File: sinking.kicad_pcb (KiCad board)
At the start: 2 copper layers, 1 part

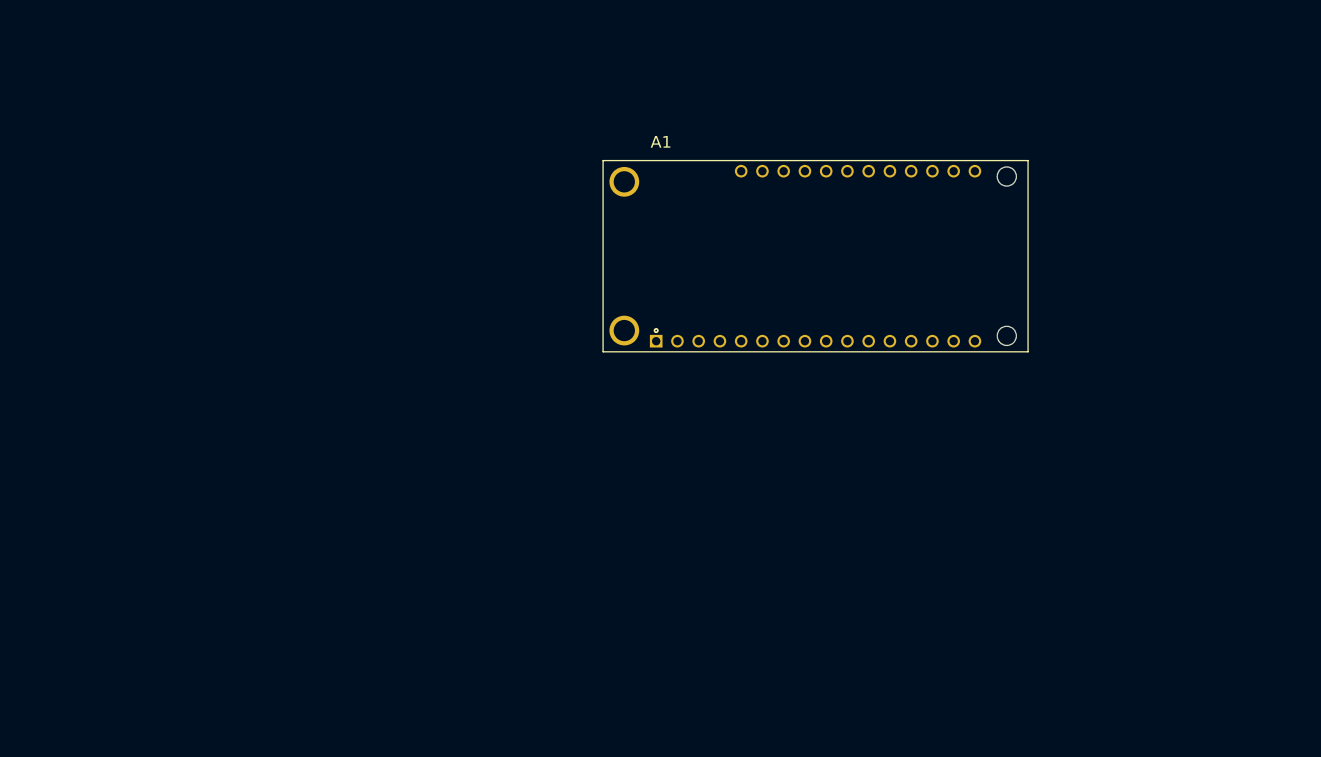
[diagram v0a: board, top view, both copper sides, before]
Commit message: improve pump input filter. add simulation
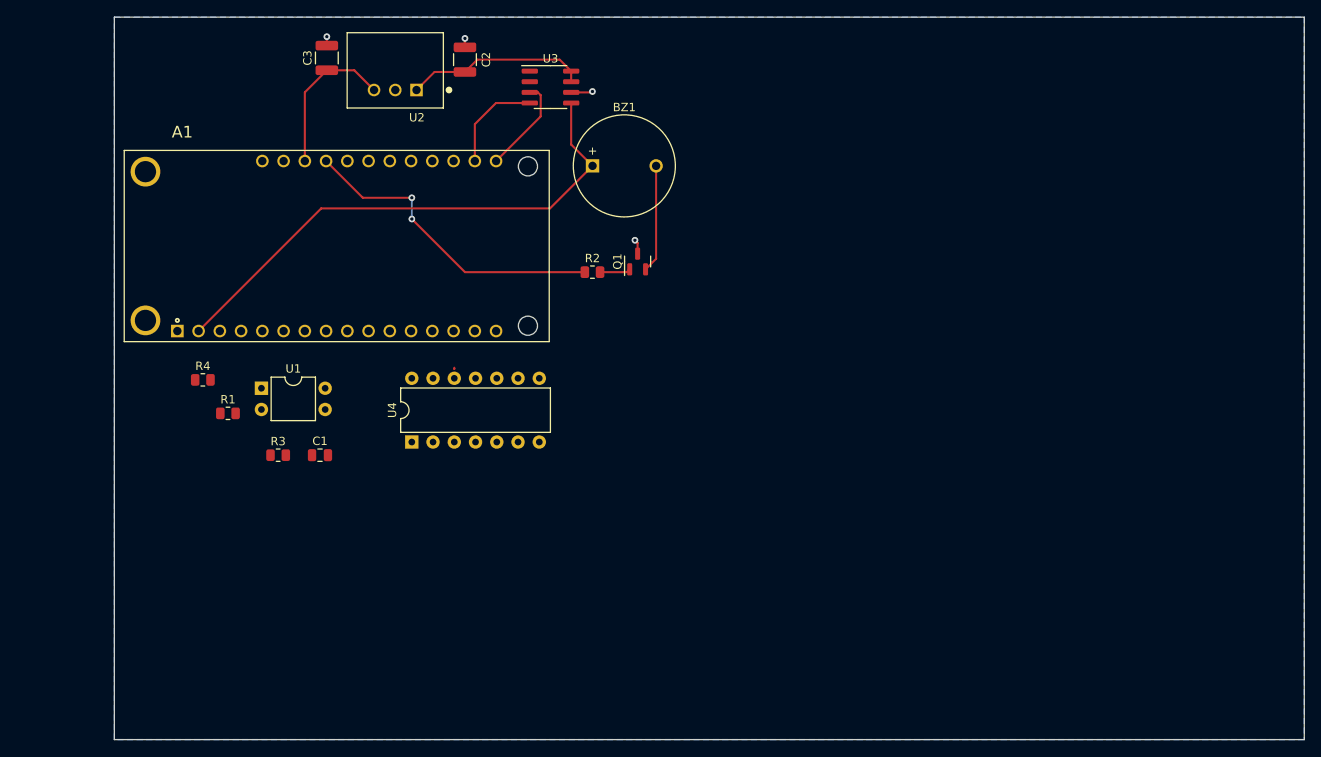
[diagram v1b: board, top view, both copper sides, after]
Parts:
- added BZ1: Buzzer, Buzzer_Beeper:MagneticBuzzer_ProSignal_ABI-009-RC, F.Cu at (115.6, 58.4)
- added C1: 1u, Capacitor_SMD:C_0805_2012Metric, F.Cu at (83.0, 93.0)
- added C2: 10u, Capacitor_SMD:C_1210_3225Metric, F.Cu at (100.3, 45.7)
- added C3: 22u, Capacitor_SMD:C_1210_3225Metric, F.Cu at (83.8, 45.5)
- added Q1: Q_NPN_BCE, Package_TO_SOT_SMD:SOT-23, F.Cu at (121.0, 69.8)
- added R1: 5k, Resistor_SMD:R_0805_2012Metric, F.Cu at (72.0, 88.0)
- added R2: 1k, Resistor_SMD:R_0805_2012Metric, F.Cu at (115.6, 71.1)
- added R3: 10k, Resistor_SMD:R_0805_2012Metric, F.Cu at (78.0, 93.0)
- added R4: 5k, Resistor_SMD:R_0805_2012Metric, F.Cu at (69.0, 84.0)
- added U1: LTV-817, Package_DIP:DIP-4_W7.62mm, F.Cu at (76.0, 85.0)
- added U2: V7805-1000, libs:CONV_V7805-1000, F.Cu at (92.0, 47.0)
- added U3: INA219AxD, Package_SO:SOIC-8_3.9x4.9mm_P1.27mm, F.Cu at (110.6, 49.0)
- added U4: 74HC14, Package_DIP:DIP-14_W7.62mm, F.Cu at (94.0, 91.4)
- moved A1 57.3 mm to (85.0, 68.0)
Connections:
- A1 pad 3V3: unconnected-(A1-Pad3V3) -> +3V3
- A1 pad D2: unconnected-(A1-SDA1_UART1_RTS_SPI1_SCK_PWM3_P1.01_2-PadD2) -> Net-(A1-SDA1_UART1_RTS_SPI1_SCK_PWM3_P1.01_2)
- A1 pad D8: unconnected-(A1-UART2_RTS_PWM1_P1.03_8-PadD8) -> Net-(A1-UART2_RTS_PWM1_P1.03_8)
- A1 pad GND: unconnected-(A1-PadGND) -> GND
- A1 pad SCL: unconnected-(A1-1_SCL_P0.27-PadSCL) -> Net-(A1-1_SCL_P0.27)
- A1 pad SDA: unconnected-(A1-0_SDA_P0.26-PadSDA) -> Net-(A1-0_SDA_P0.26)
- A1 pad VUSB: unconnected-(A1-VBUS-PadVUSB) -> VUSB
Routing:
- net +3V3: track 0.00 -> 63.8 mm
- net Net-(A1-UART2_RTS_PWM1_P1.03_8): track 0.00 -> 37.9 mm, vias 0 -> 2
- net +12V: track 0.00 -> 22.2 mm
- net VUSB: track 0.00 -> 18.6 mm
- net Net-(BZ1--): track 0.00 -> 12.9 mm
- net Net-(A1-1_SCL_P0.27): track 0.00 -> 12.0 mm
- net Net-(A1-0_SDA_P0.26): track 0.00 -> 11.5 mm
- net GND: track 0.00 -> 6.45 mm, vias 0 -> 4
- net Net-(Q1-B): track 0.00 -> 3.68 mm
- added copper zone on B.Cu, net GND
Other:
- board outline added: 142.2 x 86.4 mm

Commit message: first layout
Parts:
- removed C3: 22u, Capacitor_SMD:C_1210_3225Metric
- removed R2: 1k, Resistor_SMD:R_0805_2012Metric
- removed R3: 10k, Resistor_SMD:R_0805_2012Metric
- removed R4: 5k, Resistor_SMD:R_0805_2012Metric
- added C10: 0.1u, Capacitor_SMD:C_1210_3225Metric, F.Cu at (165.1, 95.2)
- added C11: 0.1u, Capacitor_SMD:C_1210_3225Metric, F.Cu at (164.9, 80.6)
- added C12: 1u, Capacitor_SMD:C_0805_2012Metric, F.Cu at (133.4, 104.8)
- added C13: 1u, Capacitor_SMD:C_0805_2012Metric, F.Cu at (133.4, 111.2)
- added C6: 4.7u, Capacitor_SMD:C_0805_2012Metric, F.Cu at (133.1, 66.7)
- added C7: 4.7u, Capacitor_SMD:C_0805_2012Metric, F.Cu at (126.1, 66.7)
- added C8: 4.7u, Capacitor_SMD:C_0805_2012Metric, B.Cu at (122.9, 67.3)
- added C9: 4.7u, Capacitor_SMD:C_0805_2012Metric, B.Cu at (123.2, 73.0)
- added D1: PMEG2005, Package_TO_SOT_SMD:SOT-23_Handsoldering, F.Cu at (133.4, 100.0)
- added J1: 1861975, 1891975:CONN_1861975, F.Cu at (121.4, 77.7)
- added J2: 1861975, 1891975:CONN_1861975, F.Cu at (177.2, 90.8)
- added J3: 1861946, 1891946:CONN_1861946, F.Cu at (177.2, 103.5)
- added J4: SM04B-SRSS-TB, Connector_JST:JST_SH_SM04B-SRSS-TB_1x04-1MP_P1.00mm_Horizontal, F.Cu at (166.4, 65.4)
- added JP1: SolderJumper_3_Open, Jumper:SolderJumper-3_P2.0mm_Open_TrianglePad1.0x1.5mm, B.Cu at (141.7, 76.7)
- added R10: 2.2k, Resistor_SMD:R_0805_2012Metric, F.Cu at (122.9, 68.6)
- added R11: 4.7k, Resistor_SMD:R_0805_2012Metric, B.Cu at (146.5, 78.0)
- added R12: 2.2k, Resistor_SMD:R_0805_2012Metric, F.Cu at (126.1, 69.2)
- added R13: 2.2k, Resistor_SMD:R_0805_2012Metric, B.Cu at (120.0, 69.2)
- added R14: 4.7k, Resistor_SMD:R_0805_2012Metric, B.Cu at (146.5, 81.4)
- added R15: 2.2k, Resistor_SMD:R_0805_2012Metric, B.Cu at (122.9, 69.8)
- added R16: 2.2k, Resistor_SMD:R_0805_2012Metric, B.Cu at (120.1, 74.0)
- added R17: 4.7k, Resistor_SMD:R_0805_2012Metric, B.Cu at (146.5, 84.8)
- added R18: 2.2k, Resistor_SMD:R_0805_2012Metric, B.Cu at (123.2, 75.6)
- added R19: 10k, Resistor_SMD:R_0805_2012Metric, F.Cu at (151.1, 73.9)
- added R20: 10k, Resistor_SMD:R_0805_2012Metric, F.Cu at (151.1, 77.7)
- added R21: 0.1, Resistor_SMD:R_2512_6332Metric, F.Cu at (171.5, 86.0)
- added R22: 10k, Resistor_SMD:R_0805_2012Metric, B.Cu at (167.4, 94.1)
- added R23: 10k, Resistor_SMD:R_0805_2012Metric, B.Cu at (164.5, 94.1)
- added R24: 0, Resistor_SMD:R_1210_3225Metric_Pad1.30x2.65mm_HandSolder, B.Cu at (143.5, 91.4)
- added R25: 10k, Resistor_SMD:R_0805_2012Metric, B.Cu at (167.4, 90.2)
- added R26: 0.1, Resistor_SMD:R_2512_6332Metric, F.Cu at (171.5, 77.8)
- added R27: 10k, Resistor_SMD:R_0805_2012Metric, B.Cu at (176.2, 67.9)
- added R28: 10k, Resistor_SMD:R_0805_2012Metric, B.Cu at (176.2, 69.8)
- added R29: 10k, Resistor_SMD:R_0805_2012Metric, B.Cu at (164.5, 90.2)
- added R30: 10k, Resistor_SMD:R_0805_2012Metric, B.Cu at (172.4, 67.9)
- added R31: 10k, Resistor_SMD:R_0805_2012Metric, B.Cu at (172.4, 69.8)
- added R7: 2.2k, Resistor_SMD:R_0805_2012Metric, F.Cu at (129.9, 68.6)
- added R8: 4.7k, Resistor_SMD:R_0805_2012Metric, B.Cu at (146.5, 74.6)
- added R9: 2.2k, Resistor_SMD:R_0805_2012Metric, F.Cu at (133.1, 69.2)
- added REF**: MountingHole_3.2mm_M3_ISO14580_Pad_TopBottom, MountingHole:MountingHole_3.2mm_M3_ISO14580_Pad_TopBottom, F.Cu at (182.2, 65.4)
- added REF**: MountingHole_3.2mm_M3_ISO14580_Pad_TopBottom, MountingHole:MountingHole_3.2mm_M3_ISO14580_Pad_TopBottom, F.Cu at (116.2, 65.4)
- added REF**: MountingHole_3.2mm_M3_ISO14580_Pad_TopBottom, MountingHole:MountingHole_3.2mm_M3_ISO14580_Pad_TopBottom, F.Cu at (182.2, 110.5)
- added REF**: MountingHole_3.2mm_M3_ISO14580_Pad_TopBottom, MountingHole:MountingHole_3.2mm_M3_ISO14580_Pad_TopBottom, F.Cu at (116.2, 110.5)
- added U5: TPS7A2033PDBVR, Package_TO_SOT_SMD:SOT-23-5, F.Cu at (133.4, 108.0)
- A1: footprint boron:Boron -> libs:Boron
- C1: value 1u -> 10u; footprint Capacitor_SMD:C_0805_2012Metric -> Capacitor_SMD:C_1210_3225Metric; moved to B.Cu
- C2: value 10u -> 22u; moved to B.Cu
- Q1: footprint Package_TO_SOT_SMD:SOT-23 -> Package_TO_SOT_SMD:SOT-23_Handsoldering; moved to B.Cu
- R1: value 5k -> 1k; moved to B.Cu
- U1: value LTV-817 -> V7805-1000; footprint Package_DIP:DIP-4_W7.62mm -> libs:CONV_V7805-1000
- U2: value V7805-1000 -> INA219AxD; footprint libs:CONV_V7805-1000 -> Package_SO:SOIC-8_3.9x4.9mm_P1.27mm
- U4: value 74HC14 -> TLP291-4; footprint Package_DIP:DIP-14_W7.62mm -> Package_SO:SOIC-16_4.55x10.3mm_P1.27mm
- moved U2 84.6 mm to (165.1, 89.6), turned to -90 degrees
- moved A1 66.1 mm to (148.0, 88.0), turned to 90 degrees
- moved U3 60.4 mm to (165.1, 75.0), turned to -90 degrees
- moved R1 57.9 mm to (127.6, 104.1), turned to 180 degrees
- moved C2 55.3 mm to (129.0, 93.0), turned to 180 degrees
- moved U1 55.1 mm to (130.8, 90.0), turned to -90 degrees
- moved BZ1 50.9 mm to (124.5, 108.6), turned to 90 degrees
- moved C1 46.4 mm to (129.0, 86.7), turned to 180 degrees
- moved U4 39.4 mm to (130.8, 77.5), turned to 0 degrees
- moved Q1 31.2 mm to (127.6, 100.3)
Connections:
- net Net-(BZ1--) renamed buzzer -
- A1 pad A0: unconnected-(A1-19_P0.03_PWM2_ADC0-PadA0) -> water_sense_sig
- A1 pad D2: Net-(A1-SDA1_UART1_RTS_SPI1_SCK_PWM3_P1.01_2) -> /input_filter/out
- A1 pad D3: unconnected-(A1-SCL1_UART1_CTS_SPI1_MOSI_PWM3_P1.02_3-PadD3) -> Net-(A1-SCL1_UART1_CTS_SPI1_MOSI_PWM3_P1.02_3)
- A1 pad D4: unconnected-(A1-UART2_TX_SPI1_MISO_PWM1_P1.08_4-PadD4) -> /input_filter1/out
- A1 pad D5: unconnected-(A1-UART2_RX_PWM1_P1.10_5-PadD5) -> /input_filter2/out
- A1 pad D6: unconnected-(A1-UART2_CTS_PWM1_P1.11_6-PadD6) -> /input_filter3/out
- A1 pad LI+: unconnected-(A1-LiPo+-PadLI+) -> Net-(A1-LiPo+)
- A1 pad SCL: Net-(A1-1_SCL_P0.27) -> SCL
- A1 pad SDA: Net-(A1-0_SDA_P0.26) -> SDA
- A1 pad VUSB: VUSB -> /VUSB
- BZ1 pad 1: +3V3 -> buzzer +
- C1 pad 1: Net-(C1-Pad1) -> Net-(U1-+VIN)
- C2 pad 1: +12V -> /VUSB
- R1 pad 1: Net-(R1-Pad1) -> Net-(A1-UART2_RTS_PWM1_P1.03_8)
- R1 pad 2: bilge_pump_pos -> Net-(Q1-B)
- U1 pad 1: Net-(R1-Pad1) -> Net-(U1-+VIN)
- U1 pad 3: GND -> /VUSB
- U2 pad 1: +12V -> Net-(U2-A1)
- U2 pad 2: GND -> Net-(U2-A0)
- U2 pad 3: VUSB -> SDA
- U3 pad 1: unconnected-(U3-A1-Pad1) -> Net-(U3-A1)
- U3 pad 2: unconnected-(U3-A0-Pad2) -> Net-(U3-A0)
- U3 pad 3: Net-(A1-0_SDA_P0.26) -> SDA
- U3 pad 4: Net-(A1-1_SCL_P0.27) -> SCL
- U3 pad 7: +12V -> aux_bat_sense_-
- U3 pad 8: +12V -> aux_bat_sese_+
- U4 pad 1: (no net) -> Net-(R9-Pad1)
- U4 pad 10: (no net) -> /input_filter3/out
- U4 pad 11: (no net) -> GND
- U4 pad 12: Net-(A1-SDA1_UART1_RTS_SPI1_SCK_PWM3_P1.01_2) -> /input_filter2/out
- U4 pad 13: Net-(C1-Pad1) -> GND
- U4 pad 14: +3V3 -> /input_filter1/out
- U4 pad 2: (no net) -> GND
- U4 pad 3: (no net) -> Net-(R12-Pad1)
- U4 pad 4: (no net) -> GND
- U4 pad 5: (no net) -> Net-(R15-Pad1)
- U4 pad 6: (no net) -> GND
- U4 pad 7: GND -> Net-(R18-Pad1)
- U4 pad 8: (no net) -> GND
- U4 pad 9: (no net) -> GND
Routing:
- net buzzer +: track 0.00 -> 90.6 mm
- net SDA: track 0.00 -> 72.1 mm, vias 0 -> 2
- net +3V3: track 63.8 -> 112.7 mm, vias 0 -> 5
- net SCL: track 0.00 -> 46.7 mm
- net +12V_IN_-: track 0.00 -> 44.5 mm, vias 0 -> 1
- net GND: track 6.45 -> 49.6 mm, vias 4 -> 14
- net water_sense_sig: track 0.00 -> 25.6 mm
- net Net-(R12-Pad1): track 0.00 -> 25.0 mm
- net +12V: track 22.2 -> 0.00 mm
- net engine_running: track 0.00 -> 21.1 mm
- net bilge_pump_2_running: track 0.00 -> 20.7 mm
- net aux_bat_sense_-: track 0.00 -> 19.1 mm
- net +12V_IN_+: track 0.00 -> 19.0 mm
- net aux_input: track 0.00 -> 18.9 mm
- net VUSB: track 18.6 -> 0.00 mm
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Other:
- board size 142.2 x 86.4 mm -> 72.4 x 51.4 mm
- board text added: "pump 1"

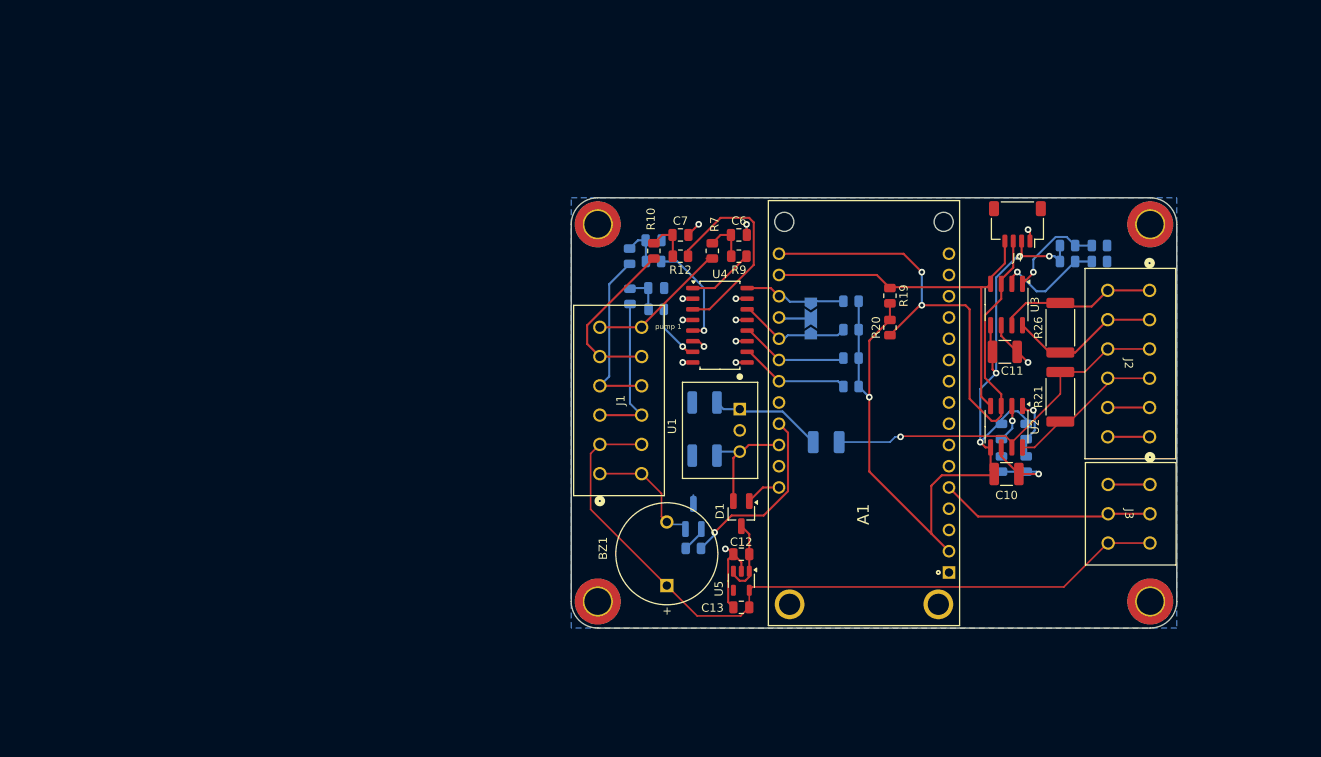
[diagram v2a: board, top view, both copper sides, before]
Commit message: add status led, etc.
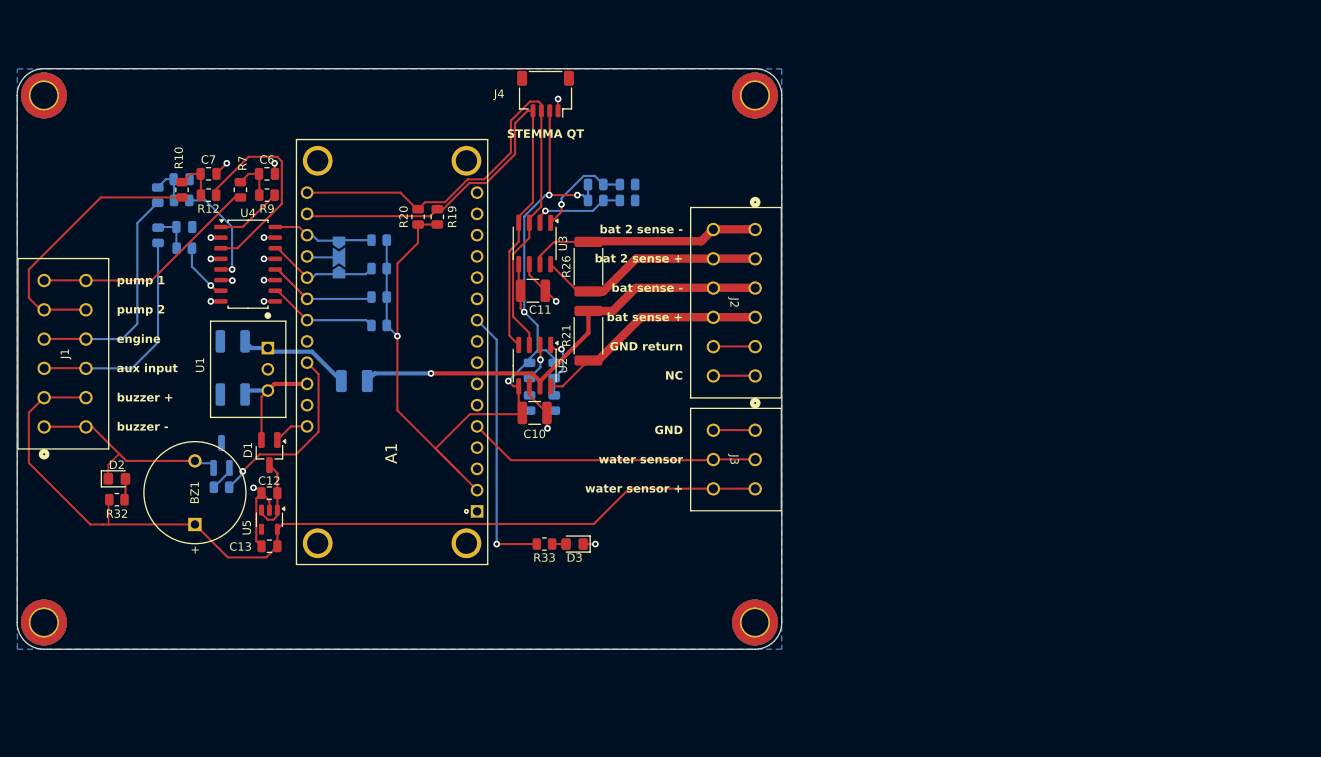
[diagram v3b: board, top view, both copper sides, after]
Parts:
- removed the REF** at (182.2, 65.4)
- removed the REF** at (116.2, 65.4)
- removed the REF** at (182.2, 110.5)
- removed the REF** at (116.2, 110.5)
- added D2: CTL0805FRD1T, LED_SMD:LED_0805_2012Metric_Pad1.15x1.40mm_HandSolder, F.Cu at (58.7, 95.8)
- added D3: LED, LED_SMD:LED_0805_2012Metric_Pad1.15x1.40mm_HandSolder, F.Cu at (113.4, 103.6)
- added R32: 330, Resistor_SMD:R_0805_2012Metric, F.Cu at (58.7, 98.3)
- added R33: 330, Resistor_SMD:R_0805_2012Metric, F.Cu at (109.8, 103.6)
- added REF**: MountingHole_3.2mm_M3_ISO14580_Pad_TopBottom, MountingHole:MountingHole_3.2mm_M3_ISO14580_Pad_TopBottom, F.Cu at (50.0, 50.0)
- added REF**: MountingHole_3.2mm_M3_ISO14580_Pad_TopBottom, MountingHole:MountingHole_3.2mm_M3_ISO14580_Pad_TopBottom, F.Cu at (135.0, 113.0)
- added REF**: MountingHole_3.2mm_M3_ISO14580_Pad_TopBottom, MountingHole:MountingHole_3.2mm_M3_ISO14580_Pad_TopBottom, F.Cu at (50.0, 113.0)
- added REF**: MountingHole_3.2mm_M3_ISO14580_Pad_TopBottom, MountingHole:MountingHole_3.2mm_M3_ISO14580_Pad_TopBottom, F.Cu at (135.0, 50.0)
- moved J1 66.7 mm to (55.0, 72.1)
- moved J4 58.5 mm to (110.0, 49.8)
- moved R20 57.9 mm to (94.7, 64.5), turned to -90 degrees
- moved A1 56.9 mm to (91.6, 80.7)
- moved C11 56.9 mm to (108.5, 73.3)
- moved C12 56.9 mm to (77.0, 97.5)
- moved C13 56.9 mm to (77.0, 103.9)
- moved C7 56.9 mm to (69.7, 59.4)
- moved C8 56.9 mm to (66.5, 60.0)
- moved D1 56.9 mm to (77.0, 92.7)
- moved JP1 56.9 mm to (85.3, 69.4)
- moved Q1 56.9 mm to (71.2, 93.0)
- moved R1 56.9 mm to (71.2, 96.8)
- moved R12 56.9 mm to (69.7, 61.9)
- moved R15 56.9 mm to (66.5, 62.5)
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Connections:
- net +12V_IN_+ renamed bat_sense_+
- net +12V_IN_- renamed bat_sense_-
- net Net-(U1-+VIN) renamed /Vin
- net aux_bat_sese_+ renamed aux_bat_sense_+
- net bilge_pump_2_running renamed bilge_pump_2
- net bilge_pump_running renamed bilge_pump
- net buzzer + renamed buzzer_+
- net buzzer - renamed buzzer_-
- A1 pad A5: unconnected-(A1-14_P0.31_PWM3_ADC5_SPI_SS-PadA5) -> Net-(A1-14_P0.31_PWM3_ADC5_SPI_SS)
- J2 pad 10: Net-(J2-Pad10) -> GND
- J2 pad 9: Net-(J2-Pad10) -> GND
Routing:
- net Net-(A1-14_P0.31_PWM3_ADC5_SPI_SS): track 0.00 -> 32.5 mm, vias 0 -> 1
- net buzzer_+: track 90.6 -> 112.6 mm
- net SCL: track 46.7 -> 65.9 mm
- net bilge_pump_2: track 20.7 -> 32.7 mm
- net +3V3: track 112.7 -> 124.4 mm
- net buzzer_-: track 14.4 -> 25.6 mm
- net bilge_pump: track 18.1 -> 27.6 mm
- net bat_sense_-: track 44.5 -> 53.9 mm
- net water_sense_sig: track 25.6 -> 34.9 mm
- net aux_bat_sense_+: track 18.2 -> 27.4 mm
- net bat_sense_+: track 19.0 -> 27.9 mm
- net aux_bat_sense_-: track 19.1 -> 28.0 mm
- net aux_input: track 18.9 -> 26.8 mm
- net engine_running: track 21.1 -> 27.4 mm
- net Net-(J2-Pad10): track 5.00 -> 0.00 mm
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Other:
- board size 72.4 x 51.4 mm -> 91.4 x 69.4 mm
- board text added: "GND"
- board text added: "GND return"
- board text added: "NC"
- board text added: "STEMMA QT"
- board text added: "aux input"
- board text added: "bat 2 sense +"
- board text added: "bat 2 sense -"
- board text added: "bat sense +"
- board text added: "bat sense -"
- board text added: "buzzer +"
- board text added: "buzzer -"
- board text added: "engine"
- board text added: "pump 2"
- board text added: "water sensor"
- board text added: "water sensor +"
